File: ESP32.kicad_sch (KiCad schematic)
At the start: 0 parts

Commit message: Insert ESP32-C6FH4
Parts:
- added BOOT1, RESET1: MOMENTARY-SWITCH-SPST-SMD-4.6X2.8MM, Thing_Plus_ESP32_C6:TACTILE_SWITCH_SMD_4.6X2.8MM, symbol Thing_Plus_ESP32_C6-eagle-import:MOMENTARY-SWITCH-SPST-SMD-4.6X2.8MM
- added C1, C2: 0.1UF-0603-25V-(+80/-20%), Thing_Plus_ESP32_C6:0603, symbol Thing_Plus_ESP32_C6-eagle-import:0.1UF-0603-25V-(+80/-20%)
- added J1: USB_C_4-LAYER_PADS, Thing_Plus_ESP32_C6:USB-C-16P_4LAYER-PADS, symbol Thing_Plus_ESP32_C6-eagle-import:USB_C_4-LAYER_PADS
- added R1, R2: 100KOHM-0603-1/10W-1%, Thing_Plus_ESP32_C6:0603, symbol Thing_Plus_ESP32_C6-eagle-import:100KOHM-0603-1/10W-1%
- added R3, R4: 5.1k, Thing_Plus_ESP32_C6:0603, symbol Thing_Plus_ESP32_C6-eagle-import:5.1KOHM5.1KOHM-0603-1/10W-1%
- added SHLD1: JUMPER-SMT_2_NC_TRACE_SILK, Thing_Plus_ESP32_C6:SMT-JUMPER_2_NC_TRACE_SILK, symbol Thing_Plus_ESP32_C6-eagle-import:JUMPER-SMT_2_NC_TRACE_SILK
- added U1: ESP32-C6-WROOM-1-NARROW, Thing_Plus_ESP32_C6:ESP32-C6-WROOM-1-NARROW, symbol uSlime:ESP32-C6-WROOM-1-NARROW
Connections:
- new net: J1.A5 (CC1), R4.2
- new net: J1.B5 (CC2), R3.2
- new net: J1.SHLD1 (SHLD), J1.SHLD2 (SHLD), J1.SHLD3 (SHLD), J1.SHLD4 (SHLD), SHLD1.1
- new net 3.3V: R1.2, R2.2, U1.2 (3V3)
- new net ESP_EN: C1.1, R2.1, RESET1.3 (2), RESET1.4 (2), U1.3 (EN)
- new net GND: BOOT1.1, BOOT1.2 (1), C1.2, C2.2, J1.GND, J1.GND2 (GND), R3.1, R4.1, RESET1.1, RESET1.2 (1), SHLD1.2, U1.1 (GND), U1.28 (GND), U1.29 (GND), U1.30 (GND), U1.31 (GND), U1.32 (GND), U1.33 (GND), U1.34 (GND), U1.35 (GND), U1.36 (GND), U1.37 (GND)
- new net IO0: U1.8 (XTAL_32K_P/IO0)
- new net IO1: U1.9 (XTAL_32K_N/IO1)
- new net IO10: U1.11 (IO10)
- new net IO11/~{ALRT}: U1.12 (IO11)
- new net IO15/LP: U1.23 (IO15)
- new net IO16/TX: U1.25 (TX0/IO16)
- new net IO17/RX: U1.24 (RX0/IO17)
- new net IO18/~{CS}: U1.16 (SDIO_CMD/IO18)
- new net IO19/SCK: U1.17 (SDIO_CLK/IO19)
- new net IO2: U1.27 (IO2)
- new net IO20/PICO: U1.18 (SDIO_D0/IO20)
- new net IO21/POCI: U1.19 (SDIO_D1/IO21)
- new net IO22/~{SD_DET}: U1.20 (SDIO_D2/IO22)
- new net IO23/STAT: U1.21 (SDIO_D3/IO23)
- new net IO3: U1.26 (IO3)
- new net IO4: U1.4 (MTMS/LP_RX/IO4)
- new net IO5: U1.5 (MTDI/LP_TX/IO5)
- new net IO6/SDA: U1.6 (MTCK/LP_SDA/IO6)
- new net IO7/SCL: U1.7 (MTDO/LP_SCL/IO7)
- new net IO8: R1.1, U1.10 (IO8)
- new net IO9/BOOT: BOOT1.3 (2), BOOT1.4 (2), C2.1, U1.15 (IO9)
- new net USB_N: J1.A7 (D-), J1.B7 (D-), U1.13 (USB_D-/IO12)
- new net USB_P: J1.A6 (D+), J1.B6 (D+), U1.14 (USB_D+/IO13)
- new net V_USB: J1.VBUS1 (VBUS), J1.VBUS2 (VBUS)
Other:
- note added: "To enter bootloader, hold BOOT button when ESP32 resets or powers on"
- note added: "USB Connector"
- note added: "VDD Range: 3.0V - 3.6V"

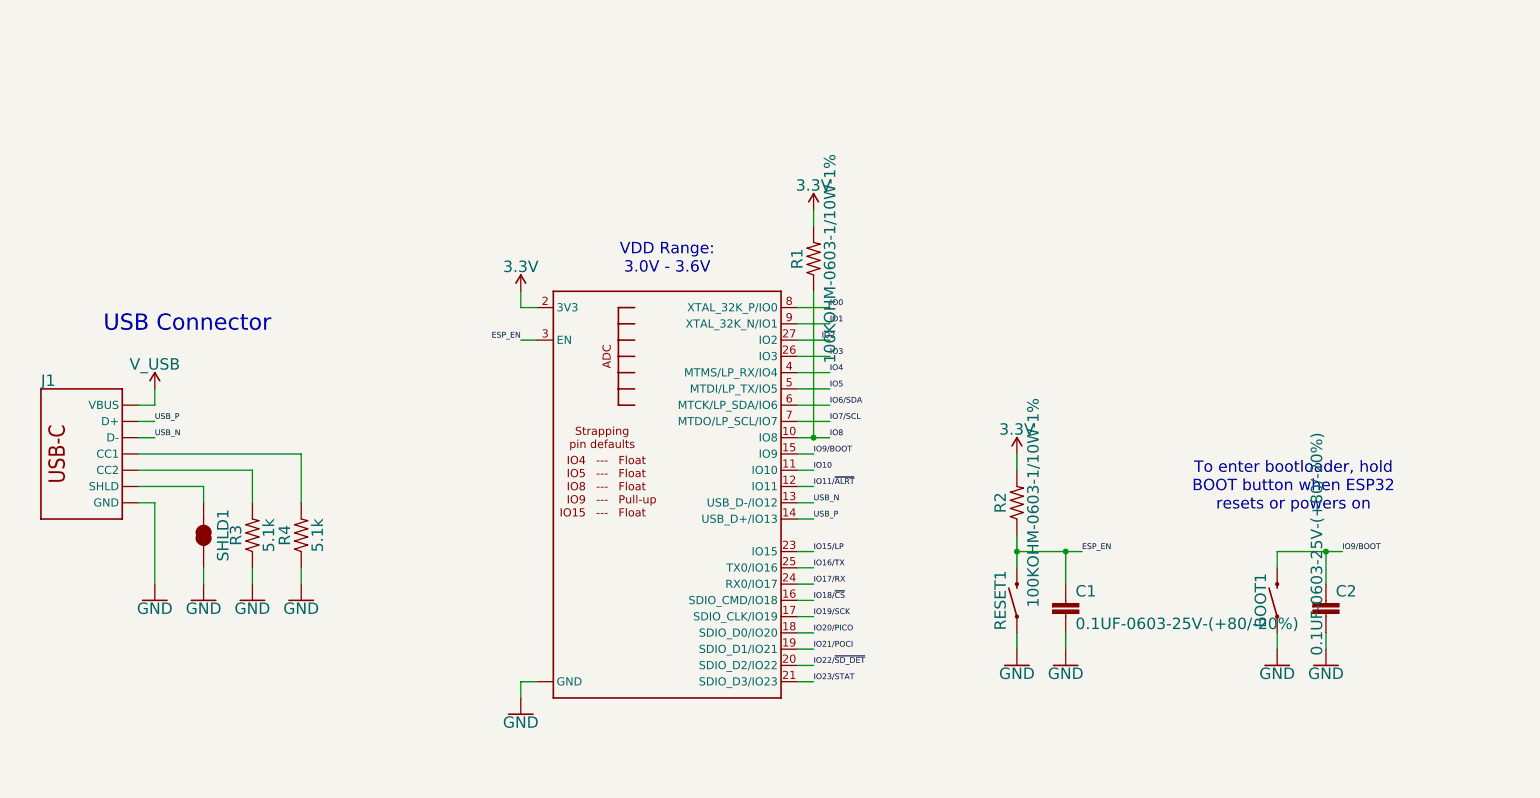
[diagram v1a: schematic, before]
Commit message: Update schematic and libraries
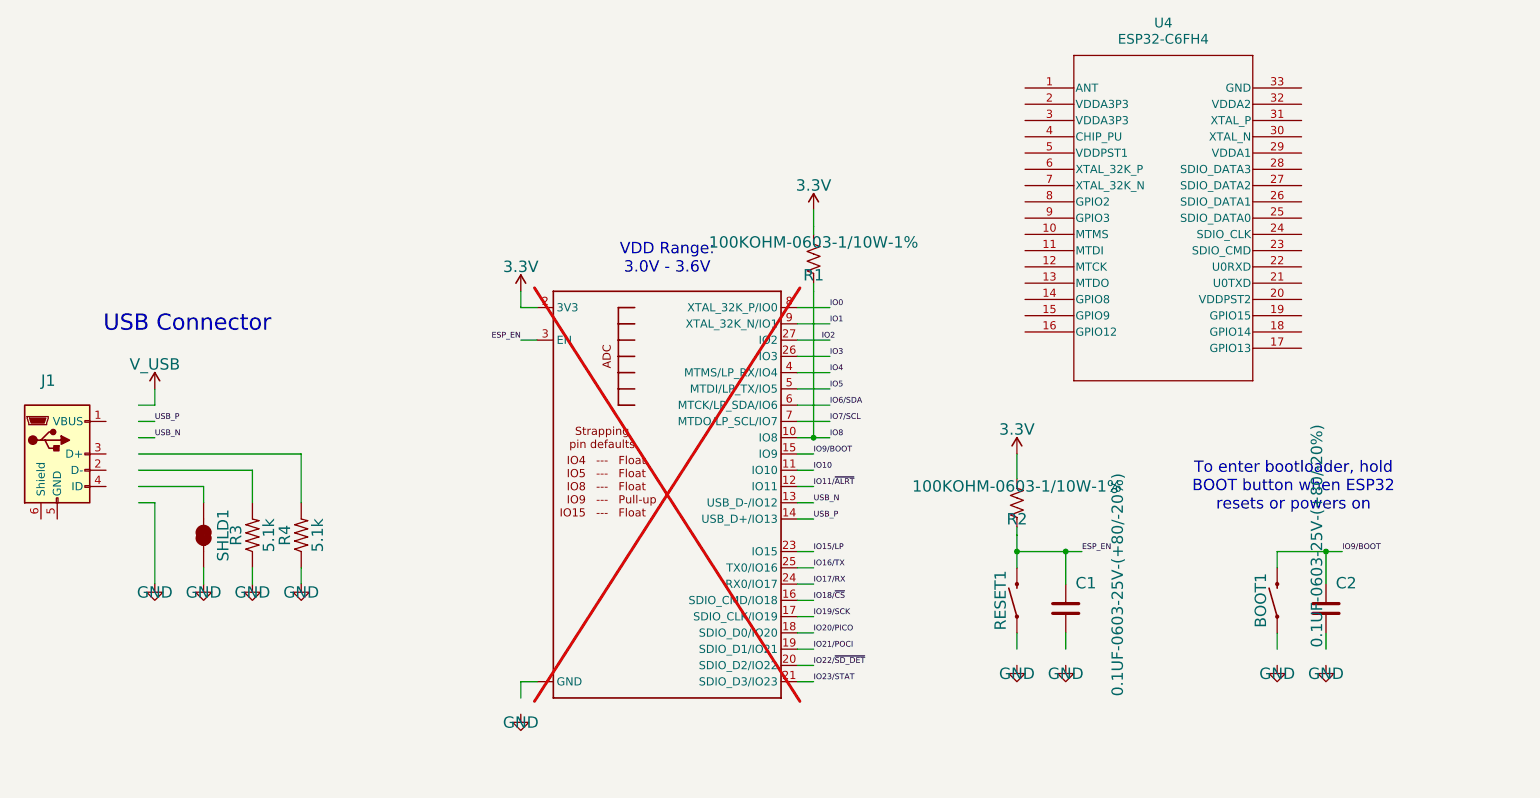
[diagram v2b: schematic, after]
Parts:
- added U4: ESP32-C6FH4, uSlime-libs:QFN32_ESP32_EXP, symbol uSlime:ESP32-C6FH4
- BOOT1, RESET1: footprint Thing_Plus_ESP32_C6:TACTILE_SWITCH_SMD_4.6X2.8MM -> Button_Switch_SMD:SW_Push_1P1T_XKB_TS-1187A
- C1, C2: footprint Thing_Plus_ESP32_C6:0603 -> Capacitor_SMD:C_0603_1608Metric; symbol Thing_Plus_ESP32_C6-eagle-import:0.1UF-0603-25V-(+80/-20%) -> uSlime:C
- J1: symbol Thing_Plus_ESP32_C6-eagle-import:USB_C_4-LAYER_PADS -> Connector:USB_B_Micro
- R1, R2: footprint Thing_Plus_ESP32_C6:0603 -> Resistor_SMD:R_0603_1608Metric; symbol Thing_Plus_ESP32_C6-eagle-import:100KOHM-0603-1/10W-1% -> uSlime:R_US
- R3, R4: footprint Thing_Plus_ESP32_C6:0603 -> Resistor_SMD:R_0603_1608Metric
- U1: now not fitted
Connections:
- net GND: no longer BOOT1.1, BOOT1.2 (1), C1.2, C2.2, J1.GND, J1.GND2 (GND), RESET1.1, RESET1.2 (1), U1.1 (GND), U1.28 (GND), U1.29 (GND), U1.30 (GND), U1.31 (GND), U1.32 (GND), U1.33 (GND), U1.34 (GND), U1.35 (GND), U1.36 (GND), U1.37 (GND)
- net USB_N: no longer J1.A7 (D-), J1.B7 (D-)
- net USB_P: no longer J1.A6 (D+), J1.B6 (D+)
- net V_USB: no longer J1.VBUS1 (VBUS), J1.VBUS2 (VBUS)
- net at R4.2: no longer J1.A5 (CC1)
- net at R3.2: no longer J1.B5 (CC2)
- new net: RESET1.1, RESET1.2 (1)
- new net: BOOT1.1, BOOT1.2 (1)
- new net: U1.1 (GND), U1.28 (GND), U1.29 (GND), U1.30 (GND), U1.31 (GND), U1.32 (GND), U1.33 (GND), U1.34 (GND), U1.35 (GND), U1.36 (GND), U1.37 (GND)
- now unconnected: SHLD1.1

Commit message: Modify ESP32
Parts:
- removed BOOT1, RESET1: MOMENTARY-SWITCH-SPST-SMD-4.6X2.8MM, Button_Switch_SMD:SW_Push_1P1T_XKB_TS-1187A, symbol Thing_Plus_ESP32_C6-eagle-import:MOMENTARY-SWITCH-SPST-SMD-4.6X2.8MM
- removed SHLD1: JUMPER-SMT_2_NC_TRACE_SILK, Thing_Plus_ESP32_C6:SMT-JUMPER_2_NC_TRACE_SILK, symbol Thing_Plus_ESP32_C6-eagle-import:JUMPER-SMT_2_NC_TRACE_SILK
- removed U4: ESP32-C6FH4, uSlime-libs:QFN32_ESP32_EXP, symbol uSlime:ESP32-C6FH4
- added BOOT1, RESET1: SW_Push, Button_Switch_SMD:SW_SPST_B3U-1000P-B, symbol uSlime:SW_Push
- J1: footprint Thing_Plus_ESP32_C6:USB-C-16P_4LAYER-PADS -> Connector_USB:USB_Micro-B_Amphenol_10103594-0001LF_Horizontal
- R3, R4: now not fitted
- U1: footprint Thing_Plus_ESP32_C6:ESP32-C6-WROOM-1-NARROW -> PCM_Espressif:ESP32-C6-MINI-1; now fitted
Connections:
- net 3.3V: no longer R1.2, U1.2 (3V3)
- net ESP_EN: now also RESET1.2
- net GND: now also C1.2, C2.2, J1.5 (GND), J1.6 (Shield), U1.1 (GND), U1.28 (GND), U1.29 (GND), U1.30 (GND), U1.31 (GND), U1.32 (GND), U1.33 (GND), U1.34 (GND), U1.35 (GND), U1.36 (GND), U1.37 (GND), BOOT1.1, RESET1.1
- net USB_N: now also J1.2 (D-)
- net USB_P: now also J1.3 (D+)
- net V_USB: now also J1.1 (VBUS)
- net IO9/BOOT renamed IO9/BOOT
- net IO9/BOOT: now also BOOT1.2
- new net +3.3V: R1.2, U1.2 (3V3)
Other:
- moved on the sheet: J1

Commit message: update power
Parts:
- removed BOOT1: SW_Push, Button_Switch_SMD:SW_SPST_B3U-1000P-B, symbol uSlime:SW_Push
- removed J1: USB_C_4-LAYER_PADS, Connector_USB:USB_Micro-B_Amphenol_10103594-0001LF_Horizontal, symbol Connector:USB_B_Micro
- removed R3, R4: 5.1k, Resistor_SMD:R_0603_1608Metric, symbol Thing_Plus_ESP32_C6-eagle-import:5.1KOHM5.1KOHM-0603-1/10W-1%
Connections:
- net USB_N renamed D- N
- net USB_P renamed D+ P
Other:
- note removed: "To enter bootloader, hold BOOT button when ESP32 resets or powers on"
- note removed: "USB Connector"
- moved on the sheet: C2

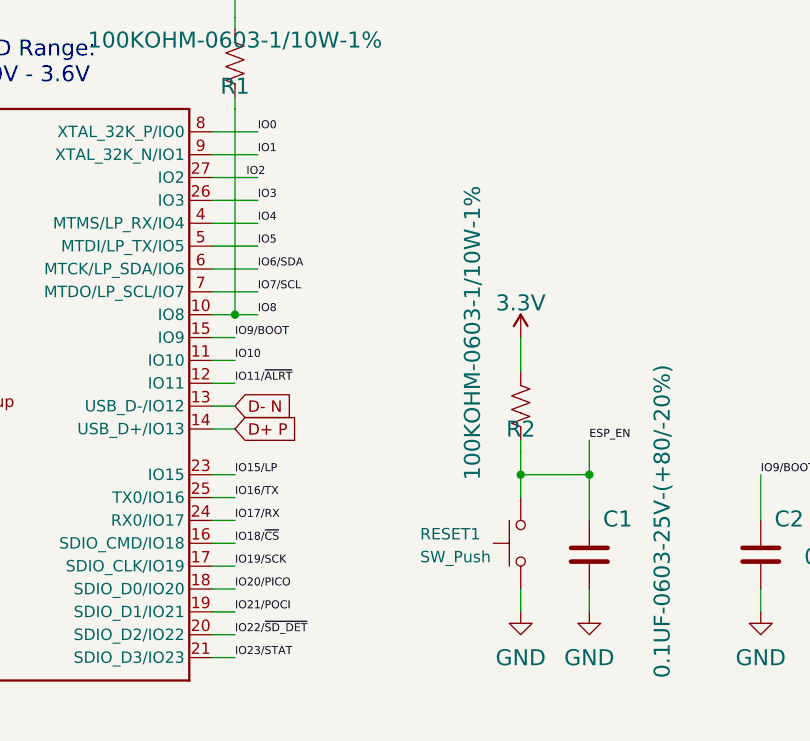
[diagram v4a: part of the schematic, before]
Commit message: Modify ESP32 connections
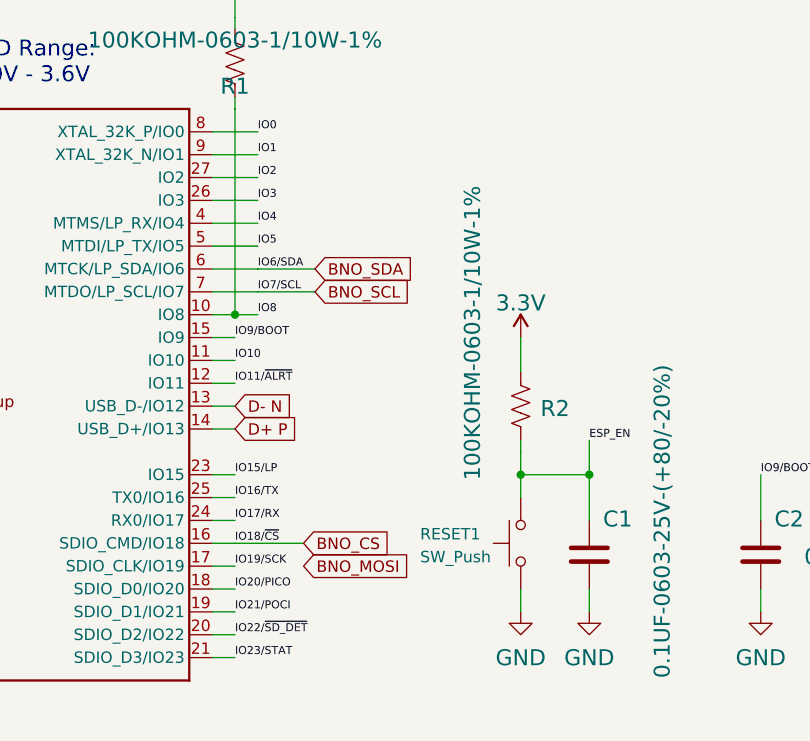
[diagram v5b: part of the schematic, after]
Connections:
- net IO18/~{CS} renamed BNO_CS
- net IO6/SDA renamed BNO_SDA
- net IO7/SCL renamed BNO_SCL
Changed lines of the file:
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@@
+	(wire
+		(pts
+			(xy 167.64 90.17) (xy 173.99 90.17)
+		)
+		(stroke
+			(width 0)
+			(type default)
+		)
+	)
+	(wire
+		(pts
+			(xy 167.64 87.63) (xy 173.99 87.63)
+		)
+		(stroke
+			(width 0)
+			(type default)
+		)
+	)
 	(wire
 		(pts
@@
 			(width 0.1524)
 			(type solid)
+		)
+	)
+	(wire
+		(pts
+			(xy 165.1 118.11) (xy 172.72 118.11)
+		)
+		(stroke
+			(width 0)
+			(type default)
 		)
 	)
@@
 	)
 	(label "IO2"
-		(at 166.37 77.47 0)
+		(at 167.64 77.47 0)
 		(fields_autoplaced yes)
 		(effects
@@
 			)
 			(justify left bottom)
+		)
+	)
+	(global_label "BNO_MOSI"
+		(shape input)
+		(at 172.72 120.65 0)
+		(fields_autoplaced yes)
+		(effects
+			(font
+				(size 1.27 1.27)
+			)
+			(justify left)
+		)
+		(property "Intersheetrefs" "${INTERSHEET_REFS}"
+			(at 185.2 120.65 0)
+			(effects
+				(font
+					(size 1.27 1.27)
+				)
+				(justify left)
+				(hide yes)
+			)
 		)
 	)
@@
 		)
 	)
+	(global_label "BNO_SCL"
+		(shape input)
+		(at 173.99 90.17 0)
+		(fields_autoplaced yes)
+		(effects
+			(font
+				(size 1.27 1.27)
+			)
+			(justify left)
+		)
+		(property "Intersheetrefs" "${INTERSHEET_REFS}"
+			(at 185.3814 90.17 0)
+			(effects
+				(font
+					(size 1.27 1.27)
+				)
+				(justify left)
+				(hide yes)
+			)
+		)
+	)
+	(global_label "BNO_SDA"
+		(shape input)
+		(at 173.99 87.63 0)
+		(fields_autoplaced yes)
+		(effects
+			(font
+				(size 1.27 1.27)
+			)
+			(justify left)
+		)
+		(property "Intersheetrefs" "${INTERSHEET_REFS}"
+			(at 185.4419 87.63 0)
+			(effects
+				(font
+					(size 1.27 1.27)
+				)
+				(justify left)
+				(hide yes)
+			)
+		)
+	)
 	(global_label "D- N"
 		(shape input)
@@
 		(property "Intersheetrefs" "${INTERSHEET_REFS}"
 			(at 173.2257 102.87 0)
+			(effects
+				(font
+					(size 1.27 1.27)
+				)
+				(justify left)
+				(hide yes)
+			)
+		)
+	)
+	(global_label "BNO_CS"
+		(shape input)
+		(at 172.72 118.11 0)
+		(fields_autoplaced yes)
+		(effects
+			(font
+				(size 1.27 1.27)
+			)
+			(justify left)
+		)
+		(property "Intersheetrefs" "${INTERSHEET_REFS}"
+			(at 183.0833 118.11 0)
 			(effects
 				(font
@@
 		(dnp no)
 		(property "Reference" "R2"
-			(at 196.85 104.394 0)
-			(effects
-				(font
+			(at 200.66 102.108 0)
+			(effects
+				(font

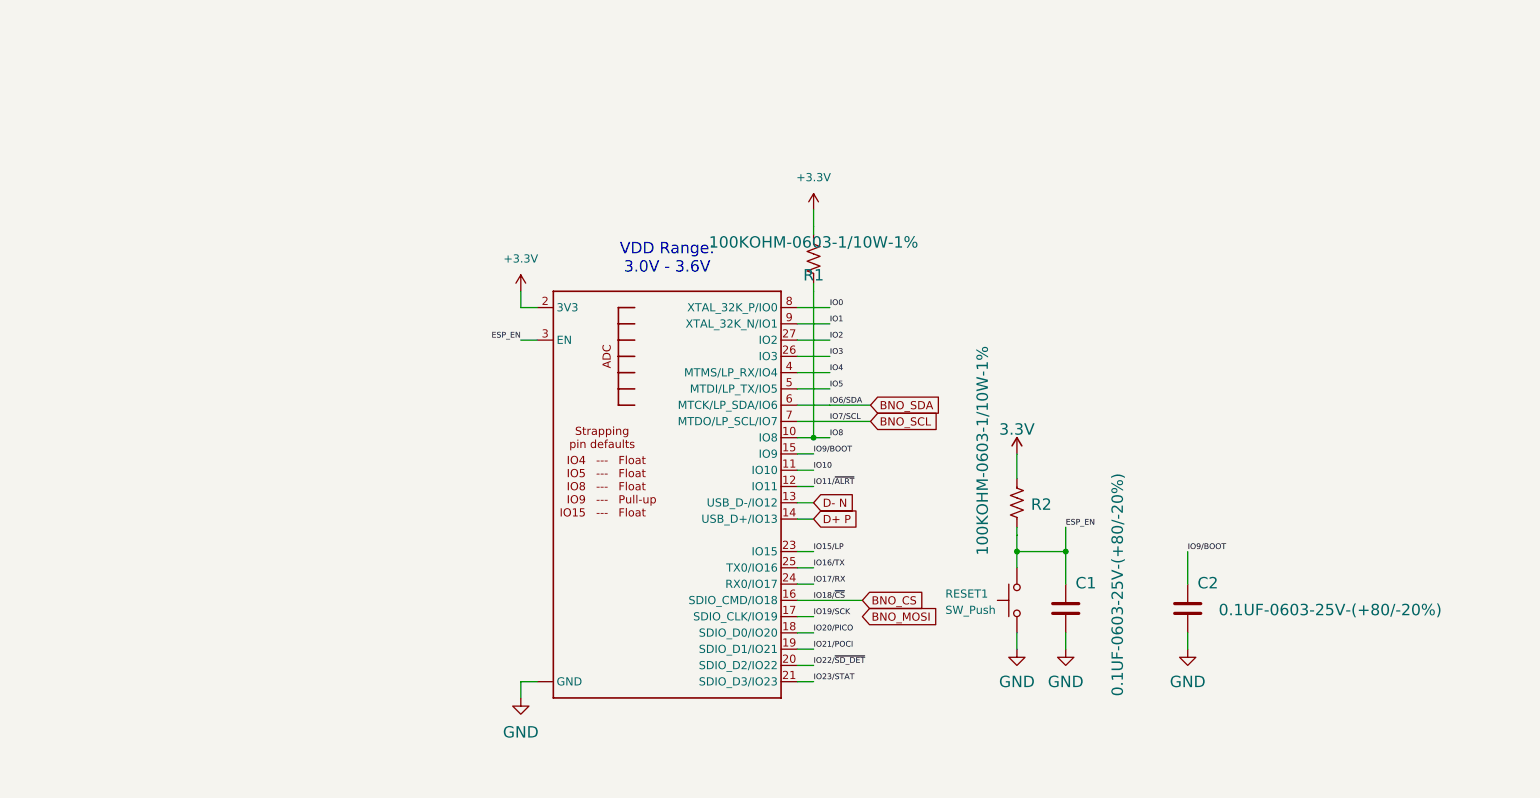
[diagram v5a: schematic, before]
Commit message: Replace ESP32 symbol with right ESP32
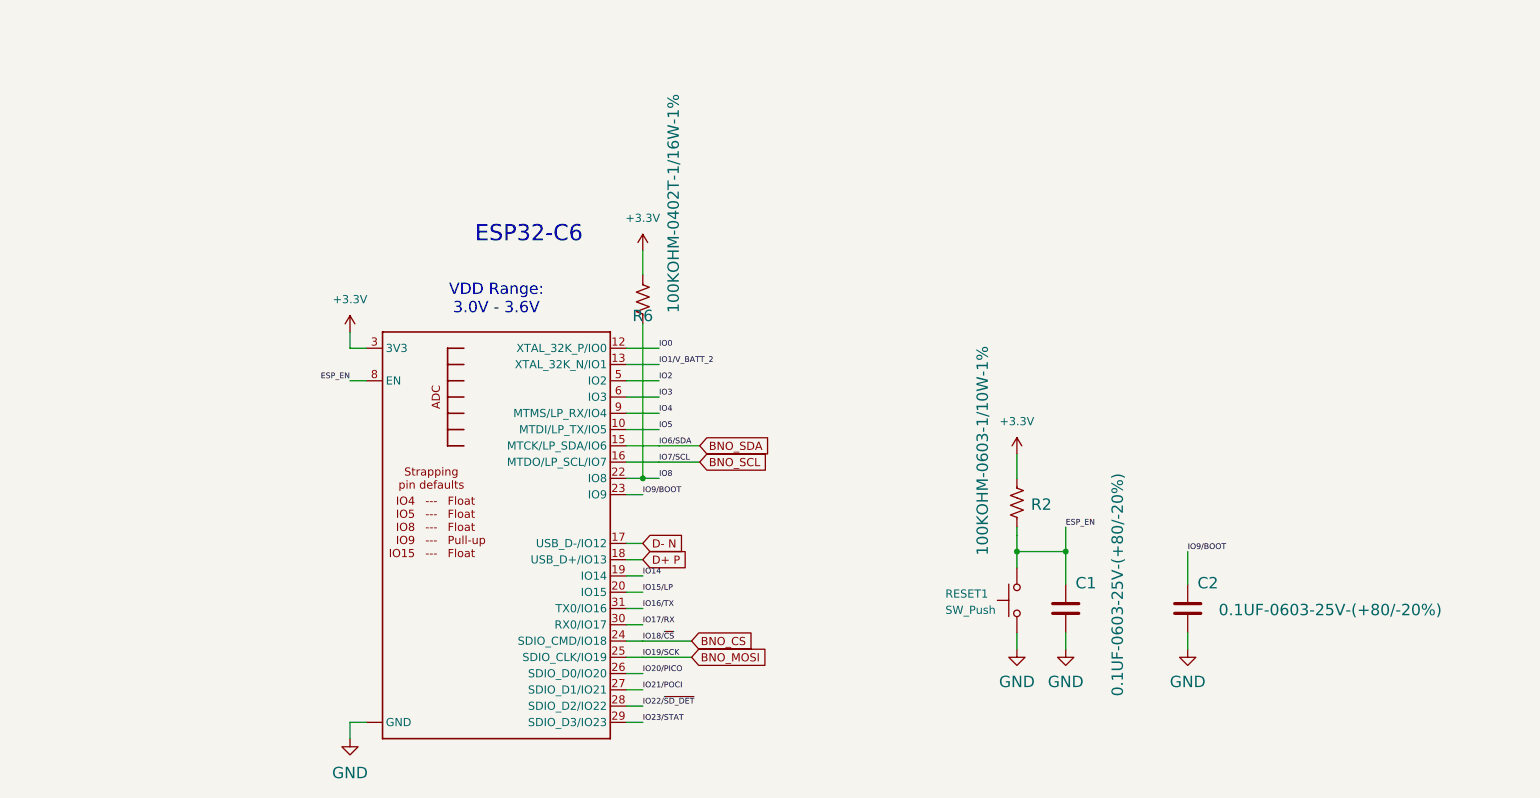
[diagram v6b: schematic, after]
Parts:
- removed R1: 100KOHM-0603-1/10W-1%, Resistor_SMD:R_0603_1608Metric, symbol uSlime:R_US
- removed U1: ESP32-C6-WROOM-1-NARROW, PCM_Espressif:ESP32-C6-MINI-1, symbol uSlime:ESP32-C6-WROOM-1-NARROW
- added R6: 100KOHM-0402T-1/16W-1%, Resistor_SMD:R_0402_1005Metric, symbol uSlime:R_US
- added U1: ESP32-C6-MINI-1, PCM_Espressif:ESP32-C6-MINI-1, symbol uSlime:ESP32-C6-MINI-1
- R2: footprint Resistor_SMD:R_0603_1608Metric -> Resistor_SMD:R_0402_1005Metric
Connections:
- net 3.3V is gone; now on net +3.3V: R2.2
- net +3.3V: now also R6.2, U1.3 (3V3)
- net BNO_CS: now also U1.24 (SDIO_CMD/IO18)
- net BNO_MOSI: now also U1.25 (SDIO_CLK/IO19)
- net BNO_SCL: now also U1.16 (MTDO/LP_SCL/IO7)
- net BNO_SDA: now also U1.15 (MTCK/LP_SDA/IO6)
- net D+ P: now also U1.18 (USB_D+/IO13)
- net D- N: now also U1.17 (USB_D-/IO12)
- net ESP_EN: now also U1.8 (EN)
- net GND: now also U1.1 (GND), U1.11 (GND), U1.14 (GND), U1.2 (GND), U1.36 (GND), U1.37 (GND), U1.38 (GND), U1.39 (GND), U1.40 (GND), U1.41 (GND), U1.42 (GND), U1.43 (GND), U1.44 (GND), U1.45 (GND), U1.46 (GND), U1.47 (GND), U1.48 (GND), U1.49 (GND), U1.50 (GND), U1.51 (GND), U1.52 (GND), U1.53 (GND)
- net IO0: now also U1.12 (XTAL_32K_P/IO0)
- net IO15/LP: now also U1.20 (IO15)
- net IO16/TX: now also U1.31 (TX0/IO16)
- net IO17/RX: now also U1.30 (RX0/IO17)
- net IO2: now also U1.5 (IO2)
- net IO20/PICO: now also U1.26 (SDIO_D0/IO20)
- net IO21/POCI: now also U1.27 (SDIO_D1/IO21)
- net IO22/~{SD_DET}: now also U1.28 (SDIO_D2/IO22)
- net IO23/STAT: now also U1.29 (SDIO_D3/IO23)
- net IO3: now also U1.6 (IO3)
- net IO4: now also U1.9 (MTMS/LP_RX/IO4)
- net IO5: now also U1.10 (MTDI/LP_TX/IO5)
- net IO8: now also R6.1, U1.22 (IO8)
- new net IO1/V_BATT_2: U1.13 (XTAL_32K_N/IO1)
- new net IO14: U1.19 (IO14)
- new net IO9/BOOT: U1.23 (IO9)
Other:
- note added: "ESP32-C6"
